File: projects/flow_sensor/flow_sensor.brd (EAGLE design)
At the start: 39.4 x 49.5 mm, 82 parts, among them J5 455-1750-1-ND

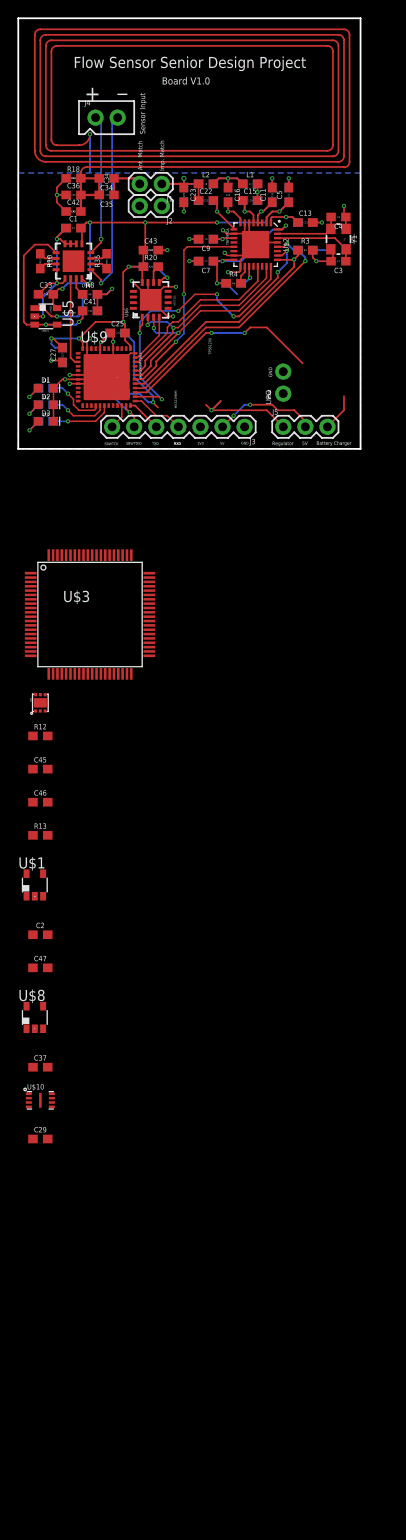
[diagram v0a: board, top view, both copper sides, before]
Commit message: Beginning v2.0 routing
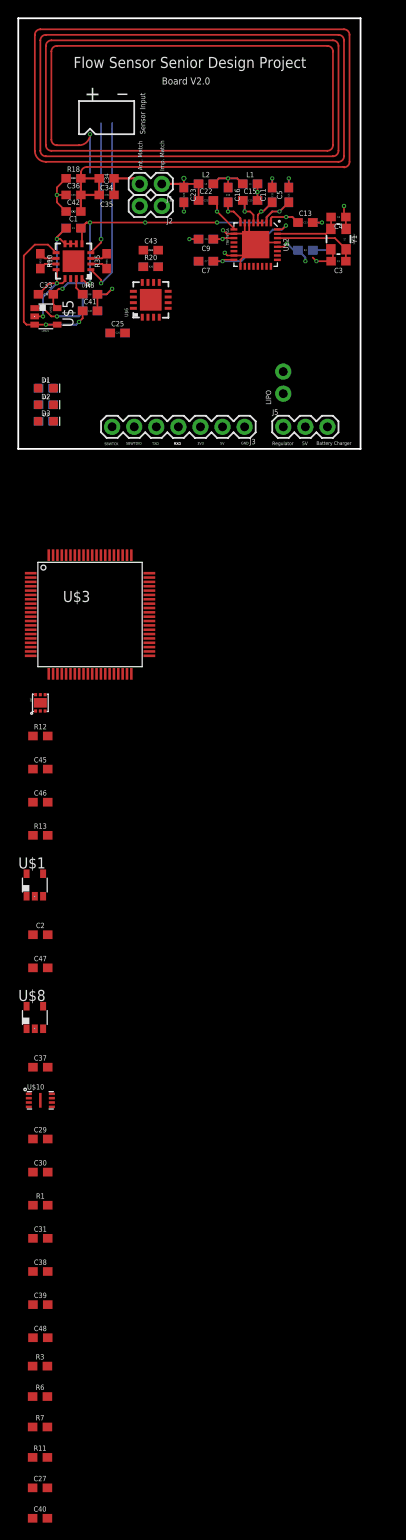
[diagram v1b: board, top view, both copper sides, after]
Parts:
- removed C44: 2.2n, SparkFun-Capacitors:0603
- removed J4: (no value), SparkFun-Connectors:1X02_NO_SILK
- removed R24: 47k, SparkFun-Resistors:0603
- removed R4, R5: 10k, SparkFun-Resistors:0603
- removed U$9: MSP430FR5994, my_library:QFN48
- added C30: 2.2n, SparkFun-Capacitors:0603
- added C31, C48: 1.0uF, SparkFun-Capacitors:0603
- added C38, C39: 0.1uF, SparkFun-Capacitors:0603
- added R1: 47k, SparkFun-Resistors:0603
- added R11, R6, R7: 10k, SparkFun-Resistors:0603
- C27: value 1.0uF -> 3.3uF
- C29: value 0.1uF -> 1uF
- C40: value 0.1uF -> 10uF
- moved C40 133.8 mm to (2.50, -123.0), flipped to the top, turned to 0 degrees
- moved R3 131.9 mm to (2.50, -105.5)
- moved C27 130.3 mm to (2.50, -119.5), turned to 0 degrees
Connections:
- removed net 11: U$3.11
- removed net 14: U$3.14
- removed net 18: U$3.18
- removed net 19: U$3.19
- removed net 49: U$3.49
- removed net 50: U$3.50
- removed net 68: U$3.68
- removed net COMMS_EN2: R3.1, U$2.25, U$9.29
- removed net N$28: J4.2, U$4.1
- removed net N$35: R22.2, U$9.17
- removed net N$5: R4.2, U$2.18
- removed net N$7: R5.2, U$2.19
- new net 3.3V: R11.1, R7.1
- new net BRIDGE_VCC: R3.2, R6.2
- new net MEM_SS: U$10.1
- new net N$1: R22.2
- new net N$18: R6.1, R7.2, U$4.1
- net CHG_STAT: no longer U$9.27
- net COMMS_EN: no longer U$9.28
- net COMMS_IRQ: no longer U$9.30
- net COMMS_SS: no longer U$9.34
- net GND: now also C27.2, C30.1, C31.1, C38.1, C39.1, C40.2, C48.1, U$3.14, U$3.19, U$3.49, U$3.68; no longer C27.1, C40.1, C44.1, R3.2, U$9.36, U$9.41, U$9.44, U$9.47, U$9.EXP
- net MISO: no longer U$9.32
- net MOSI: no longer U$9.31
- net N$29: now also R11.2, R3.1; no longer J4.1
- net N$34: no longer U$9.16
- net N$38: no longer U$9.18
- net RXD: now also U$3.41; no longer U$9.25
- net SBWTCK: now also U$3.71; no longer U$9.22
- net SBWTDIO: now also C30.2, R1.1, U$3.76; no longer C44.2, R24.1, U$9.23
- net SCK: no longer U$9.26
- net SENSOR_OUT: no longer U$9.3
- net TEMP_SS: no longer U$9.35
- net TXD: now also U$3.40; no longer U$9.24
- net VCC: now also C31.2, C38.2, C39.2, C48.2, R1.2, U$2.25, U$3.11, U$3.18, U$3.50; no longer C27.2, C40.2, R24.2, U$9.37, U$9.48
- net VCHGR: now also C40.1
- net VIN: now also C27.1, U$2.18, U$2.19; no longer R4.1, R5.1
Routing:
- net GND: track 519.9 -> 459.7 mm, vias 27 -> 14
- net VCC: track 97.3 -> 47.6 mm, vias 11 -> 6
- net SCK: track 40.4 -> 0.01 mm, vias 7 -> 0
- net COMMS_EN2: track 28.3 -> 0.00 mm, vias 1 -> 0
- net MOSI: track 26.5 -> 0.00 mm, vias 2 -> 0
- net MISO: track 25.9 -> 0.00 mm, vias 2 -> 0
- net COMMS_EN: track 30.1 -> 4.46 mm
- net CHG_STAT: track 24.1 -> 0.00 mm, vias 2 -> 0
- net COMMS_IRQ: track 23.7 -> 0.00 mm, vias 2 -> 0
- net N$28: track 21.9 -> 0.00 mm, vias 1 -> 0
- net N$18: track 0.00 -> 21.0 mm, vias 0 -> 1
- net COMMS_SS: track 20.0 -> 0.00 mm
- net VBAT: track 13.8 -> 0.90 mm, vias 1 -> 0
- net 5V: track 12.0 -> 0.00 mm, vias 2 -> 0
- net SENSOR_OUT: track 10.2 -> 0.00 mm
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- removed copper zone on layer 16, net GND
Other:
- board text added: "Board V2.0"
- board text removed: "ADT7320"
- board text removed: "Board V1.0"
- board text removed: "C27"
- board text removed: "C40"
- board text removed: "C44"
- board text removed: "MIC5219BM5"
- board text removed: "MSP430FR5994"
- board text removed: "R17"
- board text removed: "R24"
- board text removed: "R4"
- board text removed: "R5"
- board text removed: "TPS61200"
- board text removed: "Vbat"

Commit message: Tentative board v2.0 complete
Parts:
- removed LIPO: (no value), SparkFun-Connectors:1X02_NO_SILK
- removed R21, R22: 47, SparkFun-Resistors:0603
- removed R23: 20, SparkFun-Resistors:0603
- removed R35: 800, SparkFun-Resistors:0603
- removed U$1: MAX1726, my_library:SOT-23-5
- removed U$10: RM25C256C, my_library:DFN8-2X3
- removed U$3: F552X---PN80, TI_MSP430_v16:PN80
- removed U$4: AD8222, my_library:QFN16-4X4
- removed U$5: LM321, my_library:SOT-23-5
- removed U$6: ADT7320, my_library:QFN16-4X4
- removed U$7: XC6805, my_library:DFN6-1.8X2.0
- removed U$8: LTC1517-5, my_library:SOT-23-5
- added C44, C49: 0.1uF, SparkFun-Capacitors:0603
- added C50: 470nF, SparkFun-Capacitors:0603
- added J4: (no value), SparkFun-Connectors:1X02
- added R14: 680, SparkFun-Resistors:0603
- added R15: 20, SparkFun-Resistors:0603
- added R16, R17: 47, SparkFun-Resistors:0603
- added R4, R5: 10k, SparkFun-Resistors:0603
- added U1: LTC1517-5, my_library:SOT-23-5
- added U2: XC6805, my_library:DFN6-1.8X2.0
- added U3: MAX1726, my_library:SOT-23-5
- added U4: ADT7320, my_library:QFN16-4X4
- added U5: AD8222, my_library:QFN16-4X4
- added U6: LM321, my_library:SOT-23-5
- added U8: RM25C256C, my_library:DFN8-2X3
- added U9: F552X---PN80, my_library:PN80
- added Y2: 32.768kHz, SparkFun-Clocks:CRYSTAL-SMD-3.2X2.5MM
- added Y3: 4MHz, SparkFun-Clocks:CRYSTAL-SMD-3.2X2.5MM
- C1: value 0.1uF -> 3.3uF
- C10, C8: value 2.2uF -> 0.1uF
- C11: value 10nF -> 3uF
- C12: value 2.2uF -> 3uF
- C13, C9: value 10nF -> 0.1uF
- C14: value 2.2uF -> 10nF
- C15: value 1.5nF -> 2.2uF
- C16: value 1.2nF -> 10nF
- C17: value 1.2nF -> 2.2uF
- C18: value 1.5nF -> 10nF
- C19, C21: value 680pF -> 2.2uF
- C2: value 1uF -> 0.1uF
- C20: value 10pF -> 10nF
- C22: value 220pF -> 10nF
- C23: value 100pF -> 2.2uF
- C25: value 1.0uF -> 1.5nF
- C26: value 0.1uF -> 1.5nF
- C27: value 3.3uF -> 27pF
- C28: value 3uF -> 1.2nF
- C29: value 1uF -> 1.2nF
- C3: value 27pF -> 10uF
- C30: value 2.2n -> 680pF
- C31: value 1.0uF -> 10pF
- C32: value 0.1uF -> 220pF
- C33: value 0.1uF -> 680pF
- C34: value 68.0pF -> 100pF
- C35: value 1.0pF -> 27pF
- C36: value 68.0pF -> 50pF; device SparkFun-Capacitors:0603 -> my_library:TZY2_TRIM_CAP
- C37, C38: value 0.1uF -> 68pF; device SparkFun-Capacitors:0603 -> capacitor-wima:C2.5-2
- C39: value 0.1uF -> 50pF; device SparkFun-Capacitors:0603 -> my_library:TZY2_TRIM_CAP
- C4: value 27pF -> 1uF
- C40: value 10uF -> 1uF
- C41: value 3uF -> 1.0uF
- C42: value 1.0pF -> 0.1uF
- C43: value 0.1uF -> 1.0uF
- C45: value 1uF -> 2.2n
- C46, C47: value 1uF -> 47pF
- C5, C7: value 10nF -> 1uF
- C6: value 2.2uF -> 1uF
- J1: value (none) -> 1X07_CONNECTOR; device SparkFun-Connectors:1X02 -> my_library:1X07_SMD_HEADER
- J2: value (none) -> 1X03_CONNECTOR; device SparkFun-Connectors:1X02 -> my_library:1X03_SMD_HEADER
- J3: device SparkFun-Connectors:1X07 -> SparkFun-Connectors:1X02_NO_SILK
- J5: value 455-1750-1-ND -> (none); device SparkFun-Connectors:1X03 -> SparkFun-Connectors:1X02
- R1: value 47k -> 56k
- R10: value 600 -> 1k; device SparkFun-Resistors:0603 -> my_library:PVG3G_TRIM_POT
- R12: value 27k -> 10k
- R13: value 56k -> 10k
- R18: value 680 -> 47k
- R19, R20: value 10k -> 50; device SparkFun-Resistors:0603 -> my_library:PVG3G_TRIM_POT
- R2: value 10k -> 27k
- R9: value 10k -> 1k; device SparkFun-Resistors:0603 -> my_library:PVG3G_TRIM_POT
- Y1: value (none) -> 13.56MHz
- moved R7 151.0 mm to (28.6, 36.2), flipped to the bottom, turned to 270 degrees
- moved R6 149.8 mm to (8.89, 40.6)
- moved R3 149.3 mm to (33.0, 40.6)
- moved C27 147.5 mm to (33.0, 24.8), flipped to the bottom, turned to 180 degrees
- moved C40 141.8 mm to (24.1, 17.1), turned to 90 degrees
- moved R11 131.9 mm to (1.27, 15.9), flipped to the bottom, turned to 270 degrees
- moved C39 127.7 mm to (5.08, 29.2), turned to 90 degrees
- moved C31 122.8 mm to (21.6, 30.5), flipped to the bottom
- moved C38 121.3 mm to (1.91, 26.7), turned to 270 degrees
- moved C48 118.3 mm to (30.5, 12.7), flipped to the bottom, turned to 180 degrees
- moved C30 116.2 mm to (26.7, 30.5), flipped to the bottom
- moved C29 110.7 mm to (24.1, 29.2), flipped to the bottom, turned to 90 degrees
- moved R1 109.9 mm to (9.35, 22.7), flipped to the bottom, turned to 270 degrees
- moved C37 100.7 mm to (10.8, 29.2), turned to 90 degrees
- moved C2 79.8 mm to (15.2, 22.9), flipped to the bottom
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- renumbered U$2 to U7
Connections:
- removed net 20: U$3.20
- removed net 3.3V: R11.1, R7.1
- removed net 61: U$3.61
- removed net N$31: D3.A, R23.1
- removed net N$37: R35.1, U$4.2
- removed net N$40: R35.2, U$4.3
- new net N$17: D3.A, U9.77
- new net N$20: C36.P$2, C37.2, C38.1, C39.P$2, R14.1
- new net N$22: R9.2, U5.2
- new net N$25: C36.P$1, C37.1, J4.2
- new net N$28: C47.1, U9.69, Y3.3
- new net N$30: C46.1, U9.70, Y3.1
- new net N$35: R20.1, R4.1
- new net N$5: D1.A, U9.79
- new net N$7: D2.A, U9.78
- new net XIN: U9.12, Y2.1
- new net XOUT: U9.13, Y2.3
- net 3V3: now also J1.P$5; no longer J3.3
- net 5V: now also J1.P$6, J2.P$2; no longer J3.2, J5.2
- net 65: now also U9.65; no longer U$3.65
- net 66: now also U9.66; no longer U$3.66
- net 67: now also U9.67; no longer U$3.67
- net ANT: now also C31.2, C32.1, C34.1, C35.1, J4.1; no longer C20.2, C22.1, C23.1, C24.1, J1.1
- net BRIDGE_VCC: now also R5.2, U9.42; no longer R6.2
- net CHG_STAT: now also R1.2, U2.3, U9.53; no longer R13.2, U$7.3
- net COMMS_EN: now also R13.1, U9.44; no longer R2.1
- net COMMS_IRQ: now also U9.21
- net COMMS_SS: now also U9.60
- net GND: now also C1.2, C10.1, C13.1, C15.2, C16.2, C18.2, C19.2, C20.2, C22.2, C27.1, C33.2, C38.2, C39.P$1, C41.1, C43.1, C44.1, C46.2, C47.2, C49.1, C5.1, C50.1, C6.1, C7.1, C9.1, J1.P$7, J3.2, J5.1, J5.2, R13.2, R14.2, R15.1, R16.1, R17.1, R19.2, R2.1, R20.2, U1.2, U2.2, U2.PAD, U3.2, U3.4, U4.11, U4.EXP, U5.12, U5.13, U5.6, U5.7, U5.8, U5.EXP, U6.2, U8.4, U9.14, U9.19, U9.49, U9.61, U9.68; no longer C1.1, C10.2, C12.2, C13.2, C19.1, C2.1, C25.1, C26.1, C27.2, C28.2, C31.1, C32.1, C33.1, C36.1, C36.2, C38.1, C39.1, C42.2, C43.2, C46.1, C47.1, C5.2, C6.2, C7.2, C9.2, D1.C, D2.C, D3.C, J2.1, J2.2, J3.1, LIPO.2, R12.1, R18.1, R18.2, R2.2, U$1.2, U$1.4, U$10.4, U$3.14, U$3.19, U$3.49, U$3.68, U$4.12, U$4.13, U$4.6, U$4.7, U$4.8, U$5.2, U$6.11, U$6.EXP, U$7.2, U$7.PAD, U$8.2
- net MEM_SS: now also U8.1, U9.55; no longer U$10.1
- net MISO: now also U4.2, U8.2, U9.47; no longer U$10.2, U$6.2
- net MOSI: now also U4.3, U8.5, U9.46; no longer U$10.5, U$6.3
- net N$1: now also D2.C, R16.2; no longer R22.2
- net N$10: now also C27.2; no longer C4.2
- net N$11: now also C22.1, C23.1; no longer C13.1, C14.1
- net N$12: now also C25.2, C26.1; no longer C15.1, C18.2
- net N$13: now also C28.1, C30.2, C31.1; no longer C16.1, C19.2, C20.1
- net N$14: now also C28.2, C29.1; no longer C16.2, C17.1
- net N$15: now also C25.1, C26.2; no longer C15.2, C18.1
- net N$16: now also C32.2, C33.1; no longer C21.1, C22.2
- net N$18: now also R5.1, R6.2, U5.1; no longer R6.1, R7.2, U$4.1
- net N$19: now also C11.1, R12.2, U6.1; no longer C28.1, R9.2, U$5.1
- net N$2: now also C2.1, U1.5; no longer C37.1, U$8.5
- net N$21: now also C12.1, U5.9, U6.3, U6.4; no longer C41.1, U$4.9, U$5.3, U$5.4
- net N$23: now also U5.10; no longer U$4.10
- net N$24: now also U5.11; no longer U$4.11
- net N$26: now also R8.2, U4.10; no longer R20.2, U$6.10
- net N$27: now also R9.1, U5.3; no longer C34.1, C35.1, J1.2
- net N$29: now also R4.2, U5.4; no longer R11.2, U$4.4
- net N$3: now also C2.2, U1.4; no longer C37.2, U$8.4
- net N$32: now also C50.2, U9.20; no longer D2.A, R22.1
- net N$33: now also R19.1, R6.1; no longer D1.A, R21.1
- net N$34: now also D3.C, R17.2; no longer R21.2
- net N$36: now also C12.2, R11.2, R12.1; no longer C41.2, R8.2, R9.1
- net N$38: now also D1.C, R15.2; no longer R23.2
- net N$39: now also R2.2, U2.4; no longer R12.2, U$7.4
- net N$4: now also C24.1; no longer C3.1
- net N$43: now also R11.1, U5.15; no longer R8.1, U$4.15
- net N$6: now also R7.2, U4.9; no longer R19.2, U$6.9
- net N$8: now also C18.1, C19.1; no longer C10.1, C9.1
- net N$9: now also C20.1, C21.1; no longer C11.1, C12.1
- net RXD: now also J1.P$4, U9.41; no longer J3.4, U$3.41
- net SBWTCK: now also J1.P$1, U9.71; no longer J3.7, U$3.71
- net SBWTDIO: now also C45.2, J1.P$2, R18.1, U9.76; no longer C30.2, J3.6, R1.1, U$3.76
- net SCK: now also U4.1, U8.6, U9.48; no longer U$10.6, U$6.1
- net SENSOR_OUT: now also U5.14, U9.80; no longer U$4.14
- net TEMP_SS: now also U4.4, U9.43; no longer U$6.4
- net TXD: now also J1.P$3, U9.40; no longer J3.5, U$3.40
- net VBAT: now also C5.2, C6.2, J2.P$1, J3.1, U2.1, U3.1, U3.5, U9.1; no longer C2.2, C45.2, J5.1, LIPO.1, U$1.1, U$1.5, U$7.1
- net VCC: now also C10.2, C13.2, C14.1, C15.1, C40.1, C41.2, C42.2, C43.2, C44.2, C49.2, C7.2, C8.1, C9.2, R18.2, R7.1, R8.1, U3.3, U4.12, U5.16, U5.5, U6.5, U8.8, U9.11, U9.18, U9.50; no longer C1.2, C25.2, C26.2, C29.1, C31.2, C32.2, C33.2, C38.2, C39.2, C43.1, C47.2, C5.1, C6.1, R1.2, R19.1, R20.1, U$1.3, U$10.8, U$3.11, U$3.18, U$3.50, U$4.16, U$4.5, U$5.5, U$6.12
- net VCHGR: now also C3.1, C4.2, J2.P$3, R1.1, U1.3, U2.6; no longer C40.1, C46.2, J5.3, R13.1, U$7.6, U$8.3
- net VIN: now also C1.1, C16.1, C17.1, U1.1; no longer C27.1, C7.1, C8.1, U$8.1
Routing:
- net VCC: track 47.6 -> 146.0 mm, vias 6 -> 17
- net RXD: track 0.00 -> 49.9 mm, vias 0 -> 2
- net GND: track 459.7 -> 508.4 mm, vias 14 -> 29
- net SCK: track 0.01 -> 43.2 mm, vias 0 -> 4
- net TXD: track 0.00 -> 42.0 mm, vias 0 -> 2
- net BRIDGE_VCC: track 0.00 -> 41.0 mm, vias 0 -> 2
- net MISO: track 0.00 -> 37.3 mm, vias 0 -> 5
- net MOSI: track 0.00 -> 36.4 mm, vias 0 -> 3
- net SENSOR_OUT: track 0.00 -> 34.5 mm, vias 0 -> 3
- net N$29: track 15.4 -> 45.9 mm, vias 1 -> 3
- net TEMP_SS: track 0.00 -> 26.3 mm, vias 0 -> 1
- net SBWTDIO: track 0.00 -> 22.8 mm, vias 0 -> 2
- net N$18: track 21.0 -> 41.6 mm, vias 1 -> 3
- net VBAT: track 0.90 -> 21.4 mm, vias 0 -> 3
- net SBWTCK: track 0.00 -> 18.3 mm
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- added copper zone on layer 16, net GND
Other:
- board text added: "32.768kHz"
- board text added: "4MHz"
- board text added: "C2"
- board text added: "C27"
- board text added: "C29"
- board text added: "C30"
- board text added: "C31"
- board text added: "C37"
- board text added: "C38"
- board text added: "C39"
- board text added: "C40"
- board text added: "C44"
- board text added: "C45"
- board text added: "C46"
- board text added: "C47"
- board text added: "C48"
- board text added: "C49"
- board text added: "DANGER-->"
- board text added: "GAIN1"
- board text added: "GAIN2"
- board text added: "LTC1517-5"
- board text added: "MAX1726"
- board text added: "MSP430F5529"
- board text added: "Parallel C"
- board text added: "R1"
- board text added: "R11"
- board text added: "R12"
- board text added: "R13"
- board text added: "R14"
- board text added: "R15"
- board text added: "R16"
- board text added: "R17"
- board text added: "RMC25C256C"
- board text added: "Series C"
- board text added: "XC6805"
- board text added: "chg_stat"
- board text added: "comms_irq"
- board text added: "remove battery"
- board text added: "vbat"
- board text added: "vcc"
- board text removed: "C8"
- board text removed: "R19"
- board text removed: "R20"
- board text removed: "R21"
- board text removed: "R22"
- board text removed: "R23"
- board text removed: "R3"
- board text removed: "R35"
- board text removed: "R8"
- board text removed: "Sensor Input"
- board text removed: "Y1"

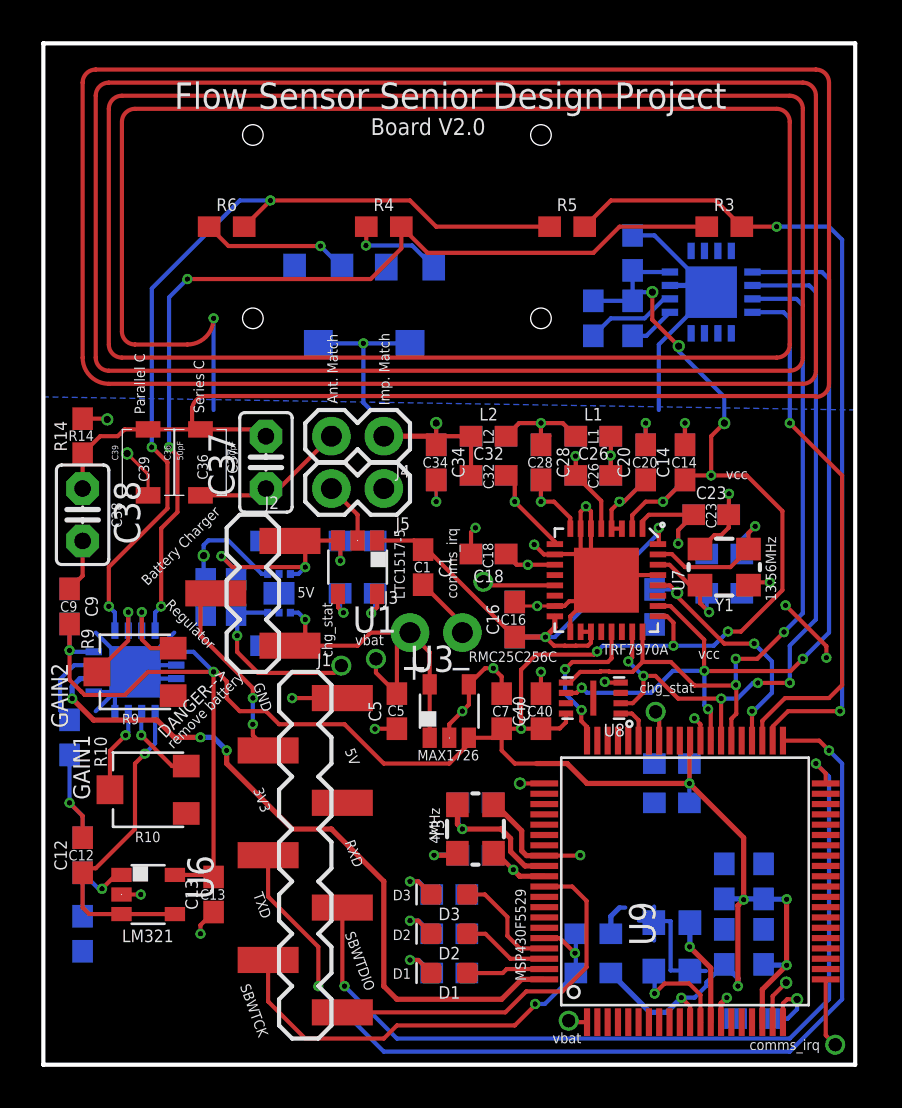
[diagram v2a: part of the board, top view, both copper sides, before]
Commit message: Replaced 32k and 4M oscillator packages, added magnetic sensors, minor rewiring; board 2 almost ready for order
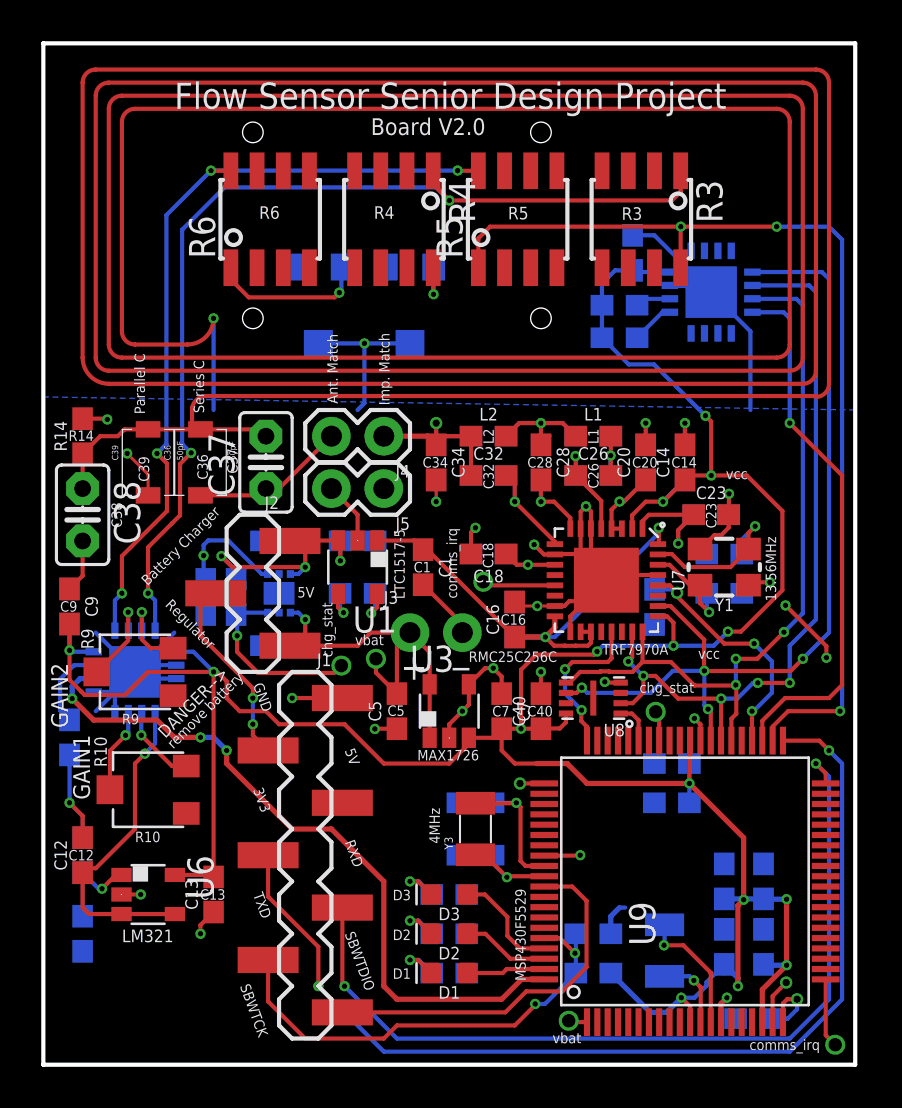
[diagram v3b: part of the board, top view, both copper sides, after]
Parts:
- R3, R4, R5, R6: value 10k -> STJ-240; device SparkFun-Resistors:0603 -> my_library:SOIC-8
- Y2, Y3: device SparkFun-Clocks:CRYSTAL-SMD-3.2X2.5MM -> my_library:CRYSTAL-3.2X1.5
- moved R3 4.04 mm to (29.0, 41.0), turned to 180 degrees
- moved R5 2.43 mm to (23.0, 41.0)
- moved R6 2.14 mm to (11.0, 41.0)
- moved R8 1.42 mm to (27.9, 36.8), turned to 180 degrees
- moved R7 1.13 mm to (27.9, 35.3), turned to 180 degrees
- moved R4 0.61 mm to (17.0, 41.0), turned to 180 degrees
- moved Y2 0.40 mm to (30.1, 5.54), turned to 270 degrees
- turned C47 to 0 degrees
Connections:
- net BRIDGE_VCC: now also R3.8, R5.1; no longer R3.2, R5.2
- net N$18: now also R3.1, R4.1, U5.4; no longer R5.1, R6.2, U5.1
- net N$28: now also Y3.P$2; no longer Y3.3
- net N$29: now also R5.8, R6.8, U5.1; no longer R3.1, R4.2, U5.4
- net N$30: now also Y3.P$1; no longer Y3.1
- net N$35: now also R4.8; no longer R4.1
- net XIN: now also Y2.P$2; no longer Y2.1
- net XOUT: now also Y2.P$1; no longer Y2.3
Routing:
- net GND: track 508.4 -> 494.3 mm, vias 29 -> 28
- net BRIDGE_VCC: track 41.0 -> 48.8 mm, vias 2 -> 3
- net N$29: track 45.9 -> 38.6 mm, vias 3 -> 4
- net N$18: track 41.6 -> 48.9 mm
- net N$26: track 4.46 -> 1.72 mm
- net N$35: track 4.64 -> 2.61 mm
- net XIN: track 5.09 -> 3.69 mm
- net VCC: track 146.0 -> 144.9 mm, vias 17 -> 15
- net XOUT: track 5.25 -> 6.24 mm
- net N$30: track 4.20 -> 5.15 mm
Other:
- board text added: "R3"
- board text added: "R4"
- board text added: "R5"
- board text added: "R6"
